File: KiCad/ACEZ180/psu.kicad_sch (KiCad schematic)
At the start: 31 parts

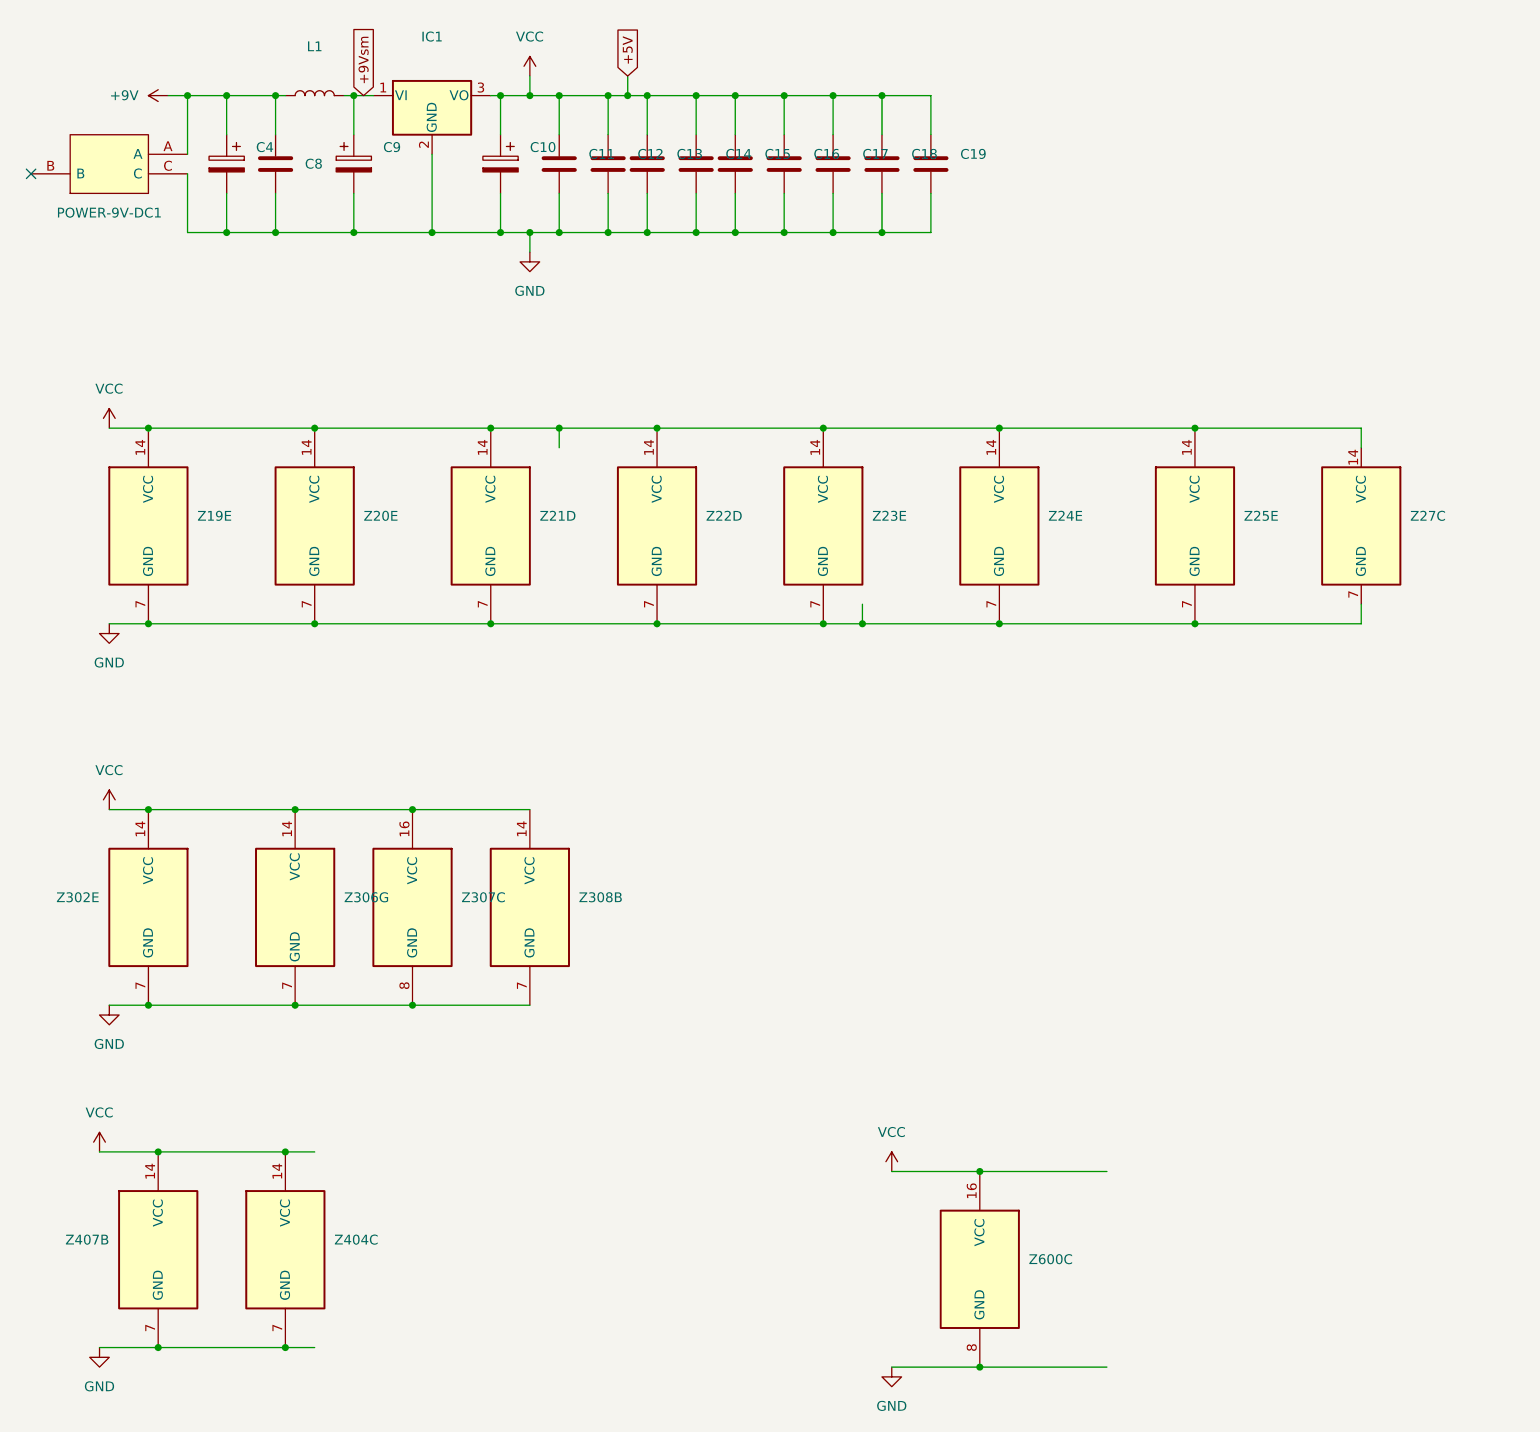
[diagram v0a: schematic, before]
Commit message: Fix mistake with ROM Select.
Signed-off-by: John Bradley <flypie@rocketmail.com>
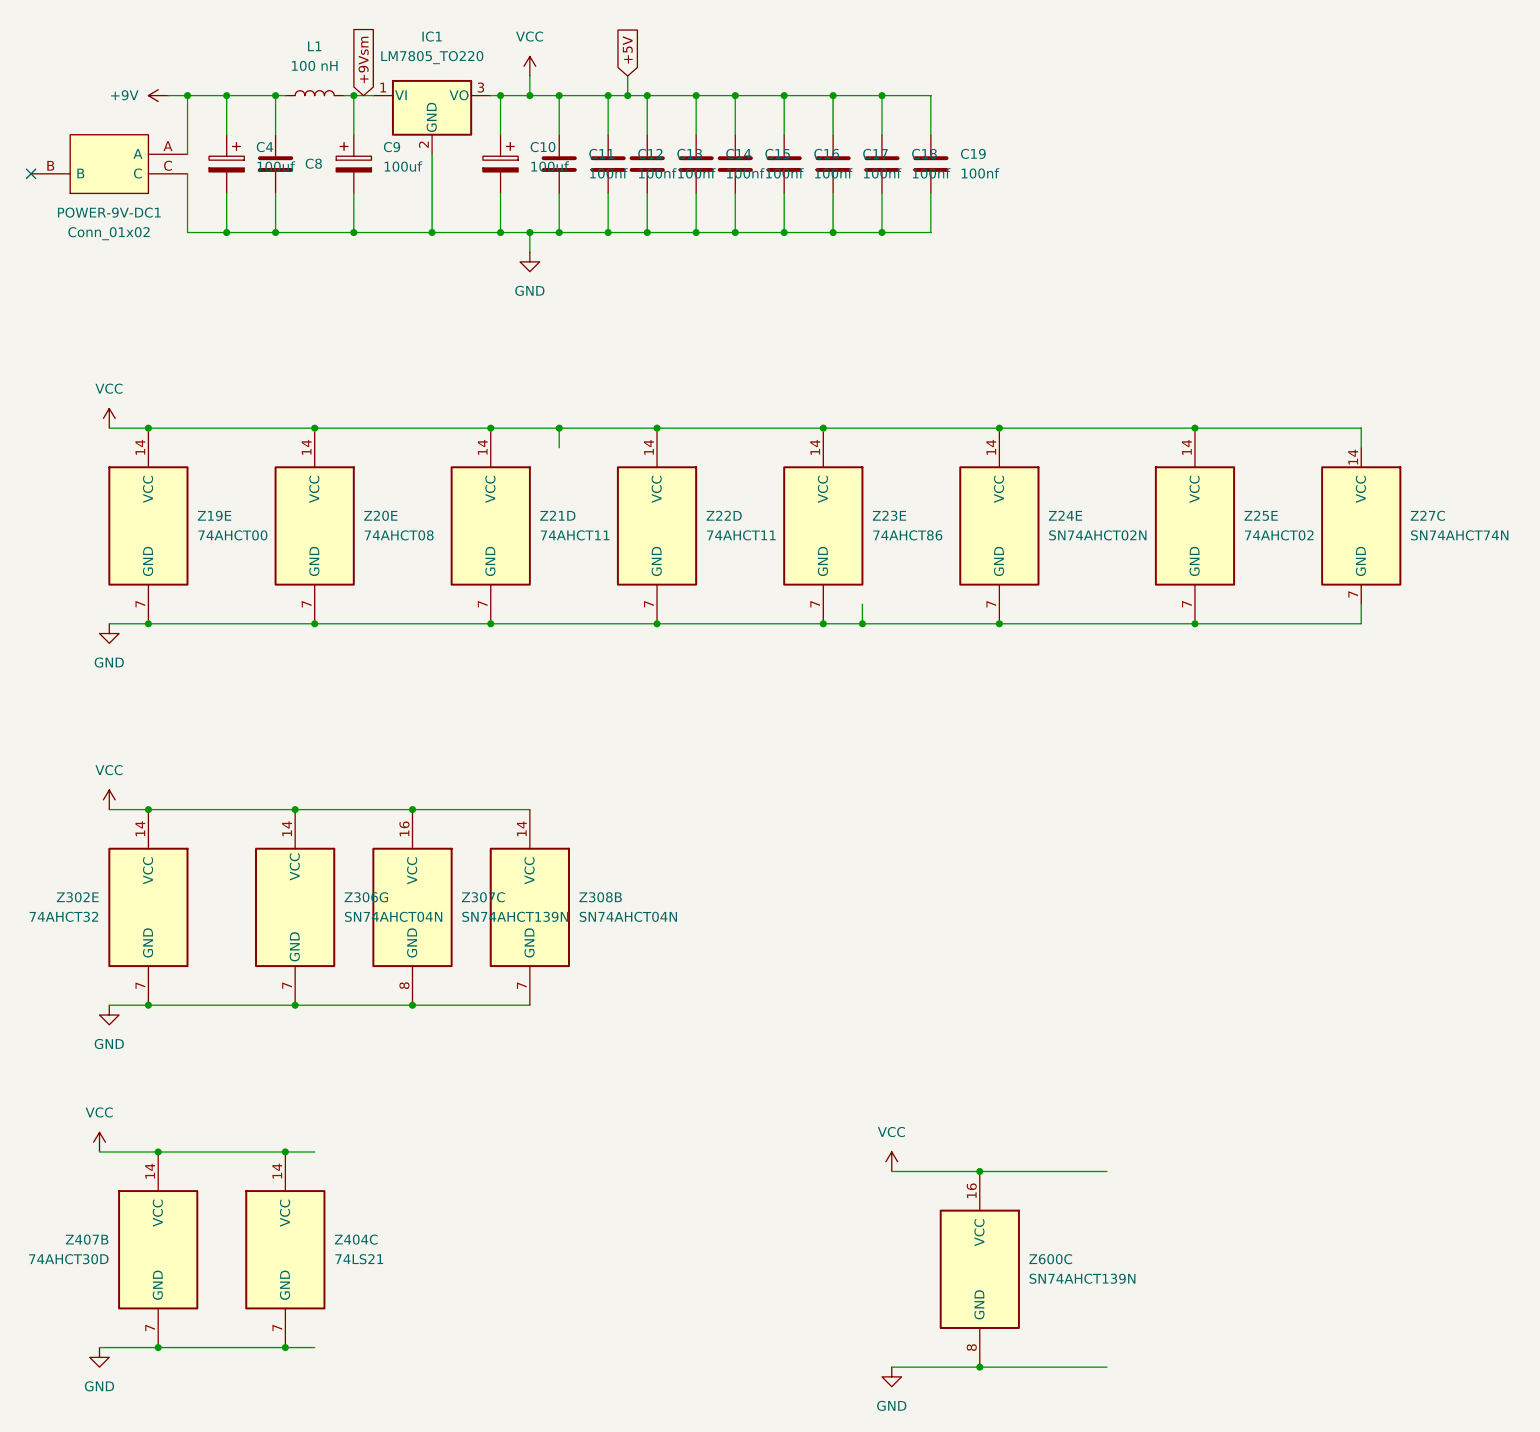
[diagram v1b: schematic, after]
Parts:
- C10, C4: value (none) -> 100uf; footprint (none) -> Capacitor_THT:CP_Radial_D5.0mm_P2.00mm
- C11, C12, C13, C14, C15, C16, C17, C18, C19, C8: value (none) -> 100nf; footprint (none) -> Capacitor_THT:C_Disc_D3.0mm_W1.6mm_P2.50mm
- C9: value (none) -> 100uf; footprint (none) -> Capacitor_THT:CP_Radial_D4.0mm_P1.50mm
- IC1: value (none) -> LM7805_TO220; footprint (none) -> Package_TO_SOT_THT:TO-220-3_Vertical
- L1: value (none) -> 100 nH; footprint (none) -> ExtraFootprints:KEMET_SBT_0260T
- POWER-9V-DC1: value (none) -> Conn_01x02; footprint (none) -> 163179PHEX
- Z19: value (none) -> 74AHCT00; footprint (none) -> Package_DIP:DIP-14_W7.62mm_Socket
- Z20: value (none) -> 74AHCT08; footprint (none) -> Package_DIP:DIP-14_W7.62mm_Socket
- Z21, Z22: value (none) -> 74AHCT11; footprint (none) -> Package_DIP:DIP-14_W7.62mm_Socket
- Z23: value (none) -> 74AHCT86; footprint (none) -> Package_DIP:DIP-14_W7.62mm_Socket
- Z24: value (none) -> SN74AHCT02N; footprint (none) -> Package_DIP:DIP-14_W7.62mm_Socket
- Z25: value (none) -> 74AHCT02; footprint (none) -> Package_DIP:DIP-14_W7.62mm_Socket; Manufacturer_Name Texas Instruments -> (none); Manufacturer_Part_Number SN74AHCT00N -> (none)
- Z27: value (none) -> SN74AHCT74N; footprint (none) -> Package_DIP:DIP-14_W7.62mm_Socket
- Z302: value (none) -> 74AHCT32; footprint (none) -> Package_DIP:DIP-14_W7.62mm_Socket
- Z306: value (none) -> SN74AHCT04N; footprint (none) -> Package_DIP:DIP-14_W7.62mm_Socket
- Z307, Z600: value (none) -> SN74AHCT139N; footprint (none) -> Package_DIP:DIP-16_W7.62mm_Socket
- Z308: value (none) -> SN74AHCT04N; footprint (none) -> Package_DIP:DIP-14_W7.62mm_Socket; symbol 74xx:74LS30 -> 74xx-FIX:74LS30; Manufacturer_Name NEXPERIA -> (none); Manufacturer_Part_Number 74AHCT30D -> (none)
- Z404: value (none) -> 74LS21; footprint (none) -> Package_DIP:DIP-14_W7.62mm_Socket
- Z407: value (none) -> 74AHCT30D; footprint (none) -> Package_DIP:DIP-14_W7.62mm_Socket; symbol 74xx:74LS30 -> 74xx-FIX:74LS30
